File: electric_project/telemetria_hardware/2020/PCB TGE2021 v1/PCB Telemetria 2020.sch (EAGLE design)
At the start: 21 parts, among them IC1 INA240A1DR, IC2 MCP3221A6T-E_OTVAO, IC3 AZ1117IH-3.3TRG1, IC4 ACS758LCB-050B-PFF-T

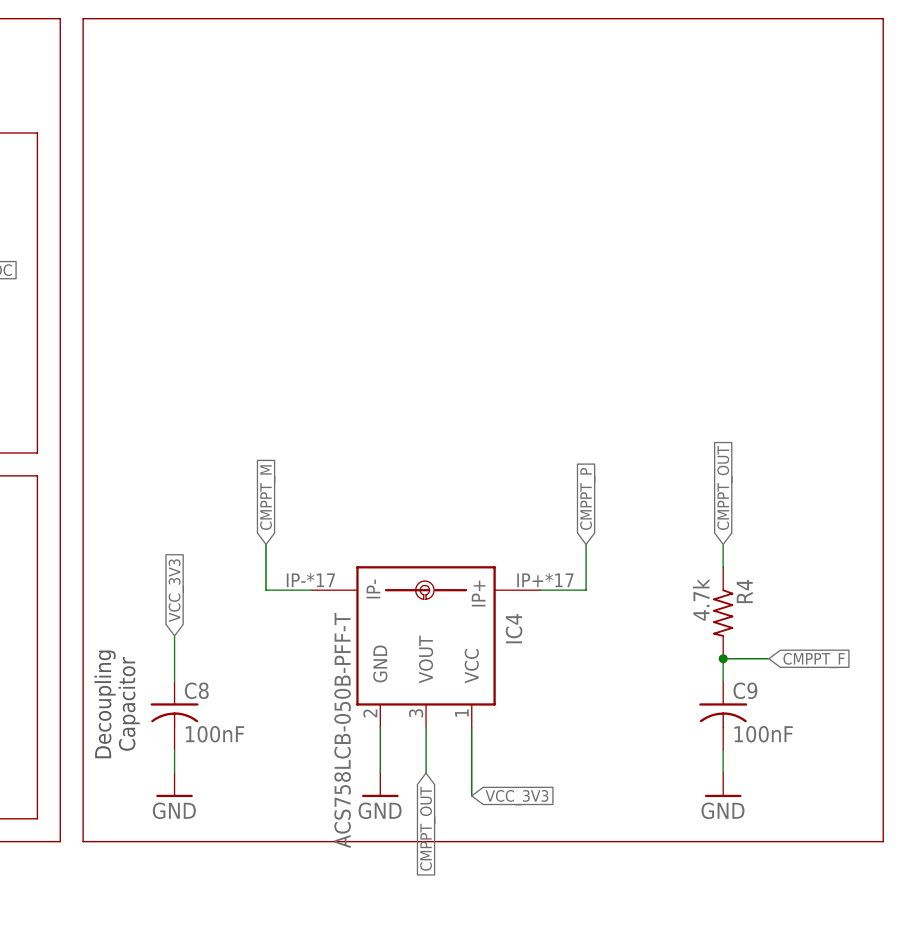
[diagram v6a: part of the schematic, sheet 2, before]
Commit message: Adding a connector to mppt current sense
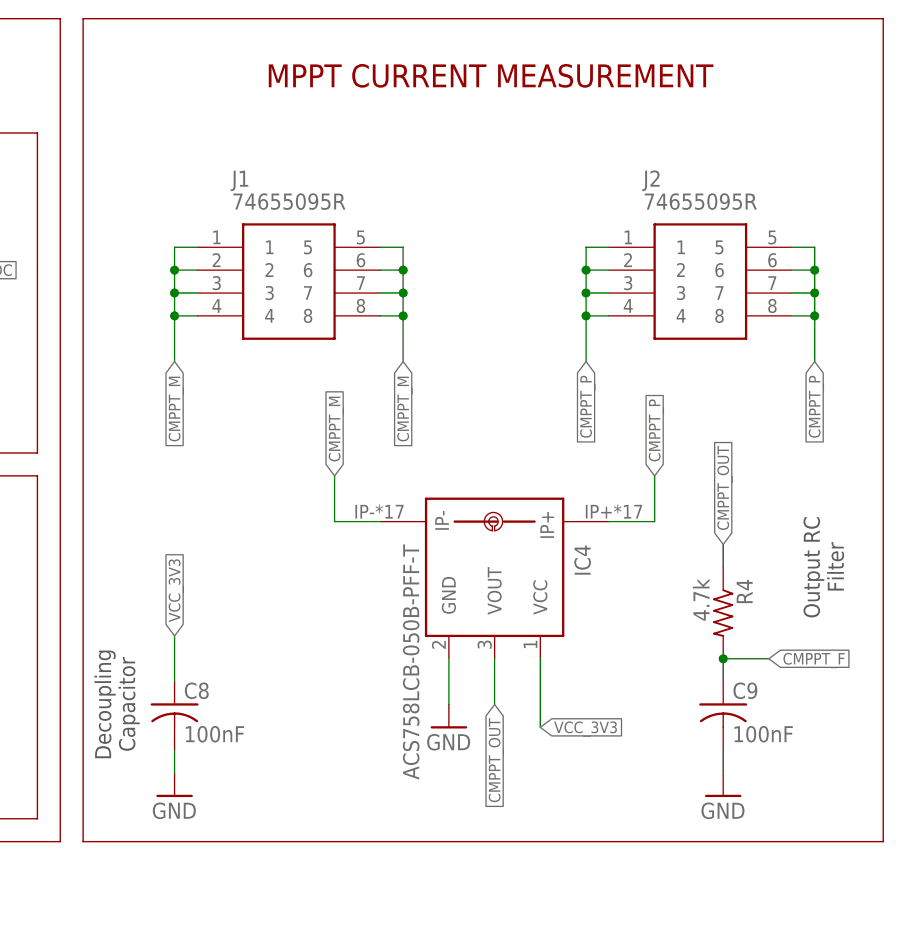
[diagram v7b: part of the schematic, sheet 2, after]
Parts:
- added J1, J2: 74655095R, SamacSys_Parts:74655095R
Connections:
- net CMPPT_M: now also J1.1, J1.2, J1.3, J1.4, J1.5, J1.6, J1.7, J1.8
- net CMPPT_P: now also J2.1, J2.2, J2.3, J2.4, J2.5, J2.6, J2.7, J2.8
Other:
- note added: "MPPT CURRENT MEASUREMENT"
- note added: "Output RC Filter"
- moved on the sheet: IC4
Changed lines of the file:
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@@
 <part name="R4" library="rcl" library_urn="urn:adsk.eagle:library:334" deviceset="R-US_" device="R0805" package3d_urn="urn:adsk.eagle:package:23553/2" value="4.7k"/>
 <part name="GND8" library="supply1" library_urn="urn:adsk.eagle:library:371" deviceset="GND" device=""/>
+<part name="J1" library="SamacSys_Parts" deviceset="74655095R" device=""/>
+<part name="J2" library="SamacSys_Parts" deviceset="74655095R" device=""/>
 </parts>
 <sheets>
@@
 <text x="161.036" y="170.18" size="1.778" layer="97" rot="R90" align="center">Decoupling
 Capacitor</text>
+<text x="177.8" y="238.76" size="2.54" layer="94">MPPT CURRENT MEASUREMENT</text>
+<text x="239.776" y="185.42" size="1.778" layer="97" rot="R90" align="center">Output RC
+Filter</text>
 </plain>
 <instances>
@@
 <attribute name="VALUE" x="129.54" y="200.66" size="1.778" layer="96"/>
 </instance>
-<instance part="IC4" gate="G$1" x="195.58" y="177.8" smashed="yes" rot="R270">
-<attribute name="NAME" x="204.47" y="180.34" size="1.778" layer="95" rot="R270"/>
-<attribute name="VALUE" x="185.42" y="180.34" size="1.778" layer="96" rot="R270"/>
-</instance>
-<instance part="GND6" gate="1" x="190.5" y="160.02" smashed="yes">
-<attribute name="VALUE" x="187.96" y="157.48" size="1.778" layer="96"/>
+<instance part="IC4" gate="G$1" x="203.2" y="185.42" smashed="yes" rot="R270">
+<attribute name="NAME" x="212.09" y="187.96" size="1.778" layer="95" rot="R270"/>
+<attribute name="VALUE" x="193.04" y="187.96" size="1.778" layer="96" rot="R270"/>
+</instance>
+<instance part="GND6" gate="1" x="198.12" y="167.64" smashed="yes">
+<attribute name="VALUE" x="195.58" y="165.1" size="1.778" layer="96"/>
 </instance>
 <instance part="C8" gate="G$1" x="167.64" y="170.18" smashed="yes">
@@
 <instance part="GND8" gate="1" x="228.6" y="160.02" smashed="yes">
 <attribute name="VALUE" x="226.06" y="157.48" size="1.778" layer="96"/>
+</instance>
+<instance part="J1" gate="G$1" x="170.18" y="220.98" smashed="yes">
+<attribute name="NAME" x="173.99" y="228.6" size="1.778" layer="95" align="center-left"/>
+<attribute name="VALUE" x="173.99" y="226.06" size="1.778" layer="96" align="center-left"/>
+</instance>
+<instance part="J2" gate="G$1" x="215.9" y="220.98" smashed="yes">
+<attribute name="NAME" x="219.71" y="228.6" size="1.778" layer="95" align="center-left"/>
+<attribute name="VALUE" x="219.71" y="226.06" size="1.778" layer="96" align="center-left"/>
 </instance>
 </instances>
@@
 <pinref part="IC4" gate="G$1" pin="GND"/>
 <pinref part="GND6" gate="1" pin="GND"/>
-<wire x1="190.5" y1="167.64" x2="190.5" y2="162.56" width="0.1524" layer="91"/>
+<wire x1="198.12" y1="175.26" x2="198.12" y2="170.18" width="0.1524" layer="91"/>
 </segment>
 <segment>
@@
 <segment>
 <pinref part="IC4" gate="G$1" pin="VCC"/>
-<label x="200.66" y="160.02" size="1.27" layer="95" xref="yes"/>
-<wire x1="200.66" y1="160.02" x2="200.66" y2="167.64" width="0.1524" layer="91"/>
+<label x="208.28" y="167.64" size="1.27" layer="95" xref="yes"/>
+<wire x1="208.28" y1="167.64" x2="208.28" y2="175.26" width="0.1524" layer="91"/>
 </segment>
 <segment>
@@
 <segment>
 <pinref part="IC4" gate="G$1" pin="VOUT"/>
-<wire x1="195.58" y1="167.64" x2="195.58" y2="162.56" width="0.1524" layer="91"/>
-<label x="195.58" y="162.56" size="1.27" layer="95" rot="R270" xref="yes"/>
+<wire x1="203.2" y1="175.26" x2="203.2" y2="170.18" width="0.1524" layer="91"/>
+<label x="203.2" y="170.18" size="1.27" layer="95" rot="R270" xref="yes"/>
 </segment>
 <segment>
@@
 <segment>
 <pinref part="IC4" gate="G$1" pin="IP+"/>
-<wire x1="208.28" y1="182.88" x2="213.36" y2="182.88" width="0.1524" layer="91"/>
-<wire x1="213.36" y1="182.88" x2="213.36" y2="187.96" width="0.1524" layer="91"/>
-<label x="213.36" y="187.96" size="1.27" layer="95" rot="R90" xref="yes"/>
+<wire x1="215.9" y1="190.5" x2="220.98" y2="190.5" width="0.1524" layer="91"/>
+<wire x1="220.98" y1="190.5" x2="220.98" y2="195.58" width="0.1524" layer="91"/>
+<label x="220.98" y="195.58" size="1.27" layer="95" rot="R90" xref="yes"/>
+</segment>
+<segment>
+<pinref part="J2" gate="G$1" pin="1"/>
+<wire x1="215.9" y1="220.98" x2="213.36" y2="220.98" width="0.1524" layer="91"/>
+<wire x1="213.36" y1="220.98" x2="213.36" y2="218.44" width="0.1524" layer="91"/>
+<wire x1="213.36" y1="218.44" x2="213.36" y2="215.9" width="0.1524" layer="91"/>
+<wire x1="213.36" y1="208.28" x2="213.36" y2="213.36" width="0.1524" layer="91"/>
+<pinref part="J2" gate="G$1" pin="3"/>
+<wire x1="213.36" y1="213.36" x2="213.36" y2="215.9" width="0.1524" layer="91"/>
+<wire x1="215.9" y1="215.9" x2="213.36" y2="215.9" width="0.1524" layer="91"/>
+<junction x="213.36" y="215.9"/>
+<pinref part="J2" gate="G$1" pin="2"/>
+<wire x1="215.9" y1="218.44" x2="213.36" y2="218.44" width="0.1524" layer="91"/>
+<junction x="213.36" y="218.44"/>
+<pinref part="J2" gate="G$1" pin="4"/>
+<wire x1="215.9" y1="213.36" x2="213.36" y2="213.36" width="0.1524" layer="91"/>
+<junction x="213.36" y="213.36"/>
+<label x="213.36" y="208.28" size="1.27" layer="95" rot="R270" xref="yes"/>
+</segment>
+<segment>
+<pinref part="J2" gate="G$1" pin="5"/>
+<wire x1="236.22" y1="220.98" x2="238.76" y2="220.98" width="0.1524" layer="91"/>
+<wire x1="238.76" y1="220.98" x2="238.76" y2="218.44" width="0.1524" layer="91"/>
+<pinref part="J2" gate="G$1" pin="8"/>
+<wire x1="238.76" y1="218.44" x2="238.76" y2="215.9" width="0.1524" layer="91"/>
+<wire x1="238.76" y1="215.9" x2="238.76" y2="213.36" width="0.1524" layer="91"/>
+<wire x1="238.76" y1="213.36" x2="238.76" y2="208.28" width="0.1524" layer="91"/>
+<wire x1="236.22" y1="213.36" x2="238.76" y2="213.36" width="0.1524" layer="91"/>
+<junction x="238.76" y="213.36"/>
+<pinref part="J2" gate="G$1" pin="7"/>
+<wire x1="236.22" y1="215.9" x2="238.76" y2="215.9" width="0.1524" layer="91"/>
+<junction x="238.76" y="215.9"/>
+<pinref part="J2" gate="G$1" pin="6"/>
+<wire x1="236.22" y1="218.44" x2="238.76" y2="218.44" width="0.1524" layer="91"/>
+<junction x="238.76" y="218.44"/>
+<label x="238.76" y="208.28" size="1.27" layer="95" rot="R270" xref="yes"/>
 </segment>
 </net>
@@
 <segment>
 <pinref part="IC4" gate="G$1" pin="IP-"/>
-<wire x1="182.88" y1="182.88" x2="177.8" y2="182.88" width="0.1524" layer="91"/>
-<wire x1="177.8" y1="182.88" x2="177.8" y2="187.96" width="0.1524" layer="91"/>
-<label x="177.8" y="187.96" size="1.27" layer="95" rot="R90" xref="yes"/>
-</segment>
-</net>
+<wire x1="190.5" y1="190.5" x2="185.42" y2="190.5" width="0.1524" layer="91"/>
+<wire x1="185.42" y1="190.5" x2="185.42" y2="195.58" width="0.1524" layer="91"/>
+<label x="185.42" y="195.58" size="1.27" layer="95" rot="R90" xref="yes"/>
+</segment>
+<segment>
+<pinref part="J1" gate="G$1" pin="1"/>
+<wire x1="170.18" y1="220.98" x2="167.64" y2="220.98" width="0.1524" layer="91"/>
+<wire x1="167.64" y1="220.98" x2="167.64" y2="218.44" width="0.1524" layer="91"/>
+<pinref part="J1" gate="G$1" pin="4"/>
+<wire x1="167.64" y1="218.44" x2="167.64" y2="215.9" width="0.1524" layer="91"/>
+<wire x1="167.64" y1="215.9" x2="167.64" y2="213.36" width="0.1524" layer="91"/>
+<wire x1="167.64" y1="213.36" x2="167.64" y2="208.28" width="0.1524" layer="91"/>
+<wire x1="170.18" y1="213.36" x2="167.64" y2="213.36" width="0.1524" layer="91"/>
+<junction x="167.64" y="213.36"/>
+<pinref part="J1" gate="G$1" pin="3"/>
+<wire x1="170.18" y1="215.9" x2="167.64" y2="215.9" width="0.1524" layer="91"/>
+<junction x="167.64" y="215.9"/>
+<pinref part="J1" gate="G$1" pin="2"/>
+<wire x1="170.18" y1="218.44" x2="167.64" y2="218.44" width="0.1524" layer="91"/>
+<junction x="167.64" y="218.44"/>
+<label x="167.64" y="208.28" size="1.27" layer="95" rot="R270" xref="yes"/>
+</segment>
+<segment>
+<pinref part="J1" gate="G$1" pin="5"/>
+<wire x1="190.5" y1="220.98" x2="193.04" y2="220.98" width="0.1524" layer="91"/>
+<wire x1="193.04" y1="220.98" x2="193.04" y2="218.44" width="0.1524" layer="91"/>
+<pinref part="J1" gate="G$1" pin="8"/>
+<wire x1="193.04" y1="218.44" x2="193.04" y2="215.9" width="0.1524" layer="91"/>
+<wire x1="193.04" y1="215.9" x2="193.04" y2="213.36" width="0.1524" layer="91"/>
+<wire x1="193.04" y1="213.36" x2="190.5" y2="213.36" width="0.1524" layer="91"/>
+<junction x="193.04" y="213.36"/>
+<pinref part="J1" gate="G$1" pin="7"/>
+<wire x1="190.5" y1="215.9" x2="193.04" y2="215.9" width="0.1524" layer="91"/>
+<junction x="193.04" y="215.9"/>
+<pinref part="J1" gate="G$1" pin="6"/>
+<wire x1="193.04" y1="218.44" x2="190.5" y2="218.44" width="0.1524" layer="91"/>
+<junction x="193.04" y="218.44"/>
+<wire x1="193.04" y1="213.36" x2="193.04" y2="208.28" width="0.1524" layer="91"/>
+<label x="193.04" y="208.28" size="1.27" layer="95" rot="R270" xref="yes"/>
+</segment>
+</net>

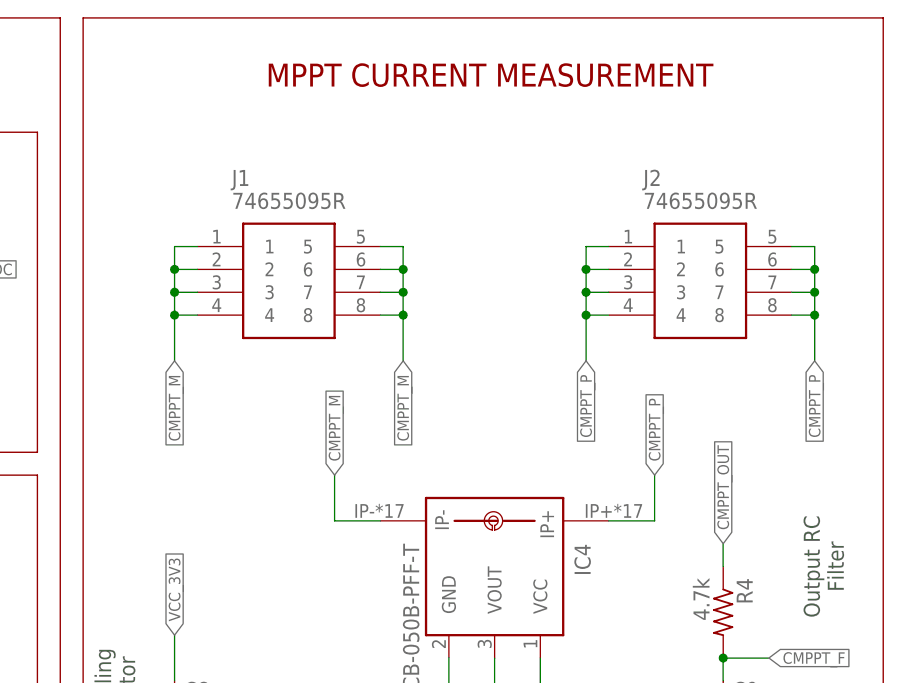
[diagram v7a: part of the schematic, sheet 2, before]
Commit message: Adding XT60 documents
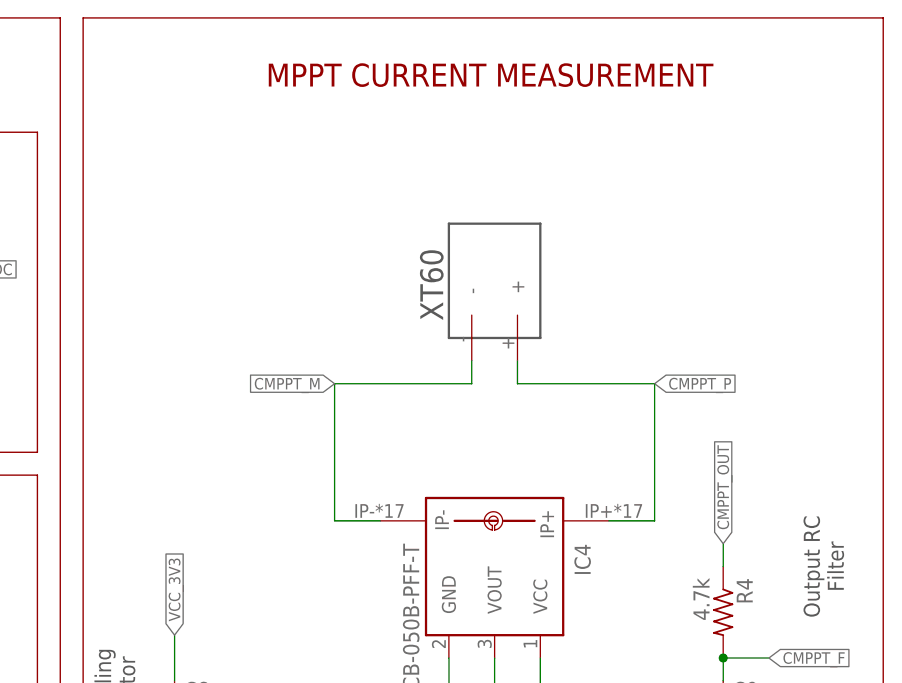
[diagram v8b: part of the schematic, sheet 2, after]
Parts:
- removed J1, J2: 74655095R, SamacSys_Parts:74655095R
- added U$3: XT60, XT60:XT60
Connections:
- net CMPPT_M: now also U$3.-; no longer J1.1, J1.2, J1.3, J1.4, J1.5, J1.6, J1.7, J1.8
- net CMPPT_P: now also U$3.+; no longer J2.1, J2.2, J2.3, J2.4, J2.5, J2.6, J2.7, J2.8
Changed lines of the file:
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@@
 <part name="R4" library="rcl" library_urn="urn:adsk.eagle:library:334" deviceset="R-US_" device="R0805" package3d_urn="urn:adsk.eagle:package:23553/2" value="4.7k"/>
 <part name="GND8" library="supply1" library_urn="urn:adsk.eagle:library:371" deviceset="GND" device=""/>
-<part name="J1" library="SamacSys_Parts" deviceset="74655095R" device=""/>
-<part name="J2" library="SamacSys_Parts" deviceset="74655095R" device=""/>
+<part name="U$3" library="XT60" deviceset="XT60" device=""/>
 </parts>
 <sheets>
@@
 <attribute name="VALUE" x="226.06" y="157.48" size="1.778" layer="96"/>
 </instance>
-<instance part="J1" gate="G$1" x="170.18" y="220.98" smashed="yes">
-<attribute name="NAME" x="173.99" y="228.6" size="1.778" layer="95" align="center-left"/>
-<attribute name="VALUE" x="173.99" y="226.06" size="1.778" layer="96" align="center-left"/>
-</instance>
-<instance part="J2" gate="G$1" x="215.9" y="220.98" smashed="yes">
-<attribute name="NAME" x="219.71" y="228.6" size="1.778" layer="95" align="center-left"/>
-<attribute name="VALUE" x="219.71" y="226.06" size="1.778" layer="96" align="center-left"/>
-</instance>
+<instance part="U$3" gate="G$1" x="203.2" y="213.36" smashed="yes" rot="R90"/>
 </instances>
 <busses>
@@
 <pinref part="IC4" gate="G$1" pin="IP+"/>
 <wire x1="215.9" y1="190.5" x2="220.98" y2="190.5" width="0.1524" layer="91"/>
-<wire x1="220.98" y1="190.5" x2="220.98" y2="195.58" width="0.1524" layer="91"/>
-<label x="220.98" y="195.58" size="1.27" layer="95" rot="R90" xref="yes"/>
-</segment>
-<segment>
-<pinref part="J2" gate="G$1" pin="1"/>
-<wire x1="215.9" y1="220.98" x2="213.36" y2="220.98" width="0.1524" layer="91"/>
-<wire x1="213.36" y1="220.98" x2="213.36" y2="218.44" width="0.1524" layer="91"/>
-<wire x1="213.36" y1="218.44" x2="213.36" y2="215.9" width="0.1524" layer="91"/>
-<wire x1="213.36" y1="208.28" x2="213.36" y2="213.36" width="0.1524" layer="91"/>
-<pinref part="J2" gate="G$1" pin="3"/>
-<wire x1="213.36" y1="213.36" x2="213.36" y2="215.9" width="0.1524" layer="91"/>
-<wire x1="215.9" y1="215.9" x2="213.36" y2="215.9" width="0.1524" layer="91"/>
-<junction x="213.36" y="215.9"/>
-<pinref part="J2" gate="G$1" pin="2"/>
-<wire x1="215.9" y1="218.44" x2="213.36" y2="218.44" width="0.1524" layer="91"/>
-<junction x="213.36" y="218.44"/>
-<pinref part="J2" gate="G$1" pin="4"/>
-<wire x1="215.9" y1="213.36" x2="213.36" y2="213.36" width="0.1524" layer="91"/>
-<junction x="213.36" y="213.36"/>
-<label x="213.36" y="208.28" size="1.27" layer="95" rot="R270" xref="yes"/>
-</segment>
-<segment>
-<pinref part="J2" gate="G$1" pin="5"/>
-<wire x1="236.22" y1="220.98" x2="238.76" y2="220.98" width="0.1524" layer="91"/>
-<wire x1="238.76" y1="220.98" x2="238.76" y2="218.44" width="0.1524" layer="91"/>
-<pinref part="J2" gate="G$1" pin="8"/>
-<wire x1="238.76" y1="218.44" x2="238.76" y2="215.9" width="0.1524" layer="91"/>
-<wire x1="238.76" y1="215.9" x2="238.76" y2="213.36" width="0.1524" layer="91"/>
-<wire x1="238.76" y1="213.36" x2="238.76" y2="208.28" width="0.1524" layer="91"/>
-<wire x1="236.22" y1="213.36" x2="238.76" y2="213.36" width="0.1524" layer="91"/>
-<junction x="238.76" y="213.36"/>
-<pinref part="J2" gate="G$1" pin="7"/>
-<wire x1="236.22" y1="215.9" x2="238.76" y2="215.9" width="0.1524" layer="91"/>
-<junction x="238.76" y="215.9"/>
-<pinref part="J2" gate="G$1" pin="6"/>
-<wire x1="236.22" y1="218.44" x2="238.76" y2="218.44" width="0.1524" layer="91"/>
-<junction x="238.76" y="218.44"/>
-<label x="238.76" y="208.28" size="1.27" layer="95" rot="R270" xref="yes"/>
+<label x="220.98" y="205.74" size="1.27" layer="95" xref="yes"/>
+<wire x1="220.98" y1="205.74" x2="220.98" y2="190.5" width="0.1524" layer="91"/>
+<pinref part="U$3" gate="G$1" pin="+"/>
+<wire x1="220.98" y1="205.74" x2="205.74" y2="205.74" width="0.1524" layer="91"/>
+<wire x1="205.74" y1="205.74" x2="205.74" y2="208.28" width="0.1524" layer="91"/>
 </segment>
 </net>
@@
 <pinref part="IC4" gate="G$1" pin="IP-"/>
 <wire x1="190.5" y1="190.5" x2="185.42" y2="190.5" width="0.1524" layer="91"/>
-<wire x1="185.42" y1="190.5" x2="185.42" y2="195.58" width="0.1524" layer="91"/>
-<label x="185.42" y="195.58" size="1.27" layer="95" rot="R90" xref="yes"/>
-</segment>
-<segment>
-<pinref part="J1" gate="G$1" pin="1"/>
-<wire x1="170.18" y1="220.98" x2="167.64" y2="220.98" width="0.1524" layer="91"/>
-<wire x1="167.64" y1="220.98" x2="167.64" y2="218.44" width="0.1524" layer="91"/>
-<pinref part="J1" gate="G$1" pin="4"/>
-<wire x1="167.64" y1="218.44" x2="167.64" y2="215.9" width="0.1524" layer="91"/>
-<wire x1="167.64" y1="215.9" x2="167.64" y2="213.36" width="0.1524" layer="91"/>
-<wire x1="167.64" y1="213.36" x2="167.64" y2="208.28" width="0.1524" layer="91"/>
-<wire x1="170.18" y1="213.36" x2="167.64" y2="213.36" width="0.1524" layer="91"/>
-<junction x="167.64" y="213.36"/>
-<pinref part="J1" gate="G$1" pin="3"/>
-<wire x1="170.18" y1="215.9" x2="167.64" y2="215.9" width="0.1524" layer="91"/>
-<junction x="167.64" y="215.9"/>
-<pinref part="J1" gate="G$1" pin="2"/>
-<wire x1="170.18" y1="218.44" x2="167.64" y2="218.44" width="0.1524" layer="91"/>
-<junction x="167.64" y="218.44"/>
-<label x="167.64" y="208.28" size="1.27" layer="95" rot="R270" xref="yes"/>
-</segment>
-<segment>
-<pinref part="J1" gate="G$1" pin="5"/>
-<wire x1="190.5" y1="220.98" x2="193.04" y2="220.98" width="0.1524" layer="91"/>
-<wire x1="193.04" y1="220.98" x2="193.04" y2="218.44" width="0.1524" layer="91"/>
-<pinref part="J1" gate="G$1" pin="8"/>
-<wire x1="193.04" y1="218.44" x2="193.04" y2="215.9" width="0.1524" layer="91"/>
-<wire x1="193.04" y1="215.9" x2="193.04" y2="213.36" width="0.1524" layer="91"/>
-<wire x1="193.04" y1="213.36" x2="190.5" y2="213.36" width="0.1524" layer="91"/>
-<junction x="193.04" y="213.36"/>
-<pinref part="J1" gate="G$1" pin="7"/>
-<wire x1="190.5" y1="215.9" x2="193.04" y2="215.9" width="0.1524" layer="91"/>
-<junction x="193.04" y="215.9"/>
-<pinref part="J1" gate="G$1" pin="6"/>
-<wire x1="193.04" y1="218.44" x2="190.5" y2="218.44" width="0.1524" layer="91"/>
-<junction x="193.04" y="218.44"/>
-<wire x1="193.04" y1="213.36" x2="193.04" y2="208.28" width="0.1524" layer="91"/>
-<label x="193.04" y="208.28" size="1.27" layer="95" rot="R270" xref="yes"/>
-</segment>
-</net>
+<label x="185.42" y="205.74" size="1.27" layer="95" rot="R180" xref="yes"/>
+<pinref part="U$3" gate="G$1" pin="-"/>
+<wire x1="200.66" y1="208.28" x2="200.66" y2="205.74" width="0.1524" layer="91"/>
+<wire x1="200.66" y1="205.74" x2="185.42" y2="205.74" width="0.1524" layer="91"/>
+<wire x1="185.42" y1="205.74" x2="185.42" y2="190.5" width="0.1524" layer="91"/>
+</segment>
+</net>
